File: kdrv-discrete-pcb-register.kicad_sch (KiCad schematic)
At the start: 3 parts, among them J1 Bus_PCI_Express_x16, J2 Bus_PCI_Express_x16, J3 Bus_PCI_Express_x16

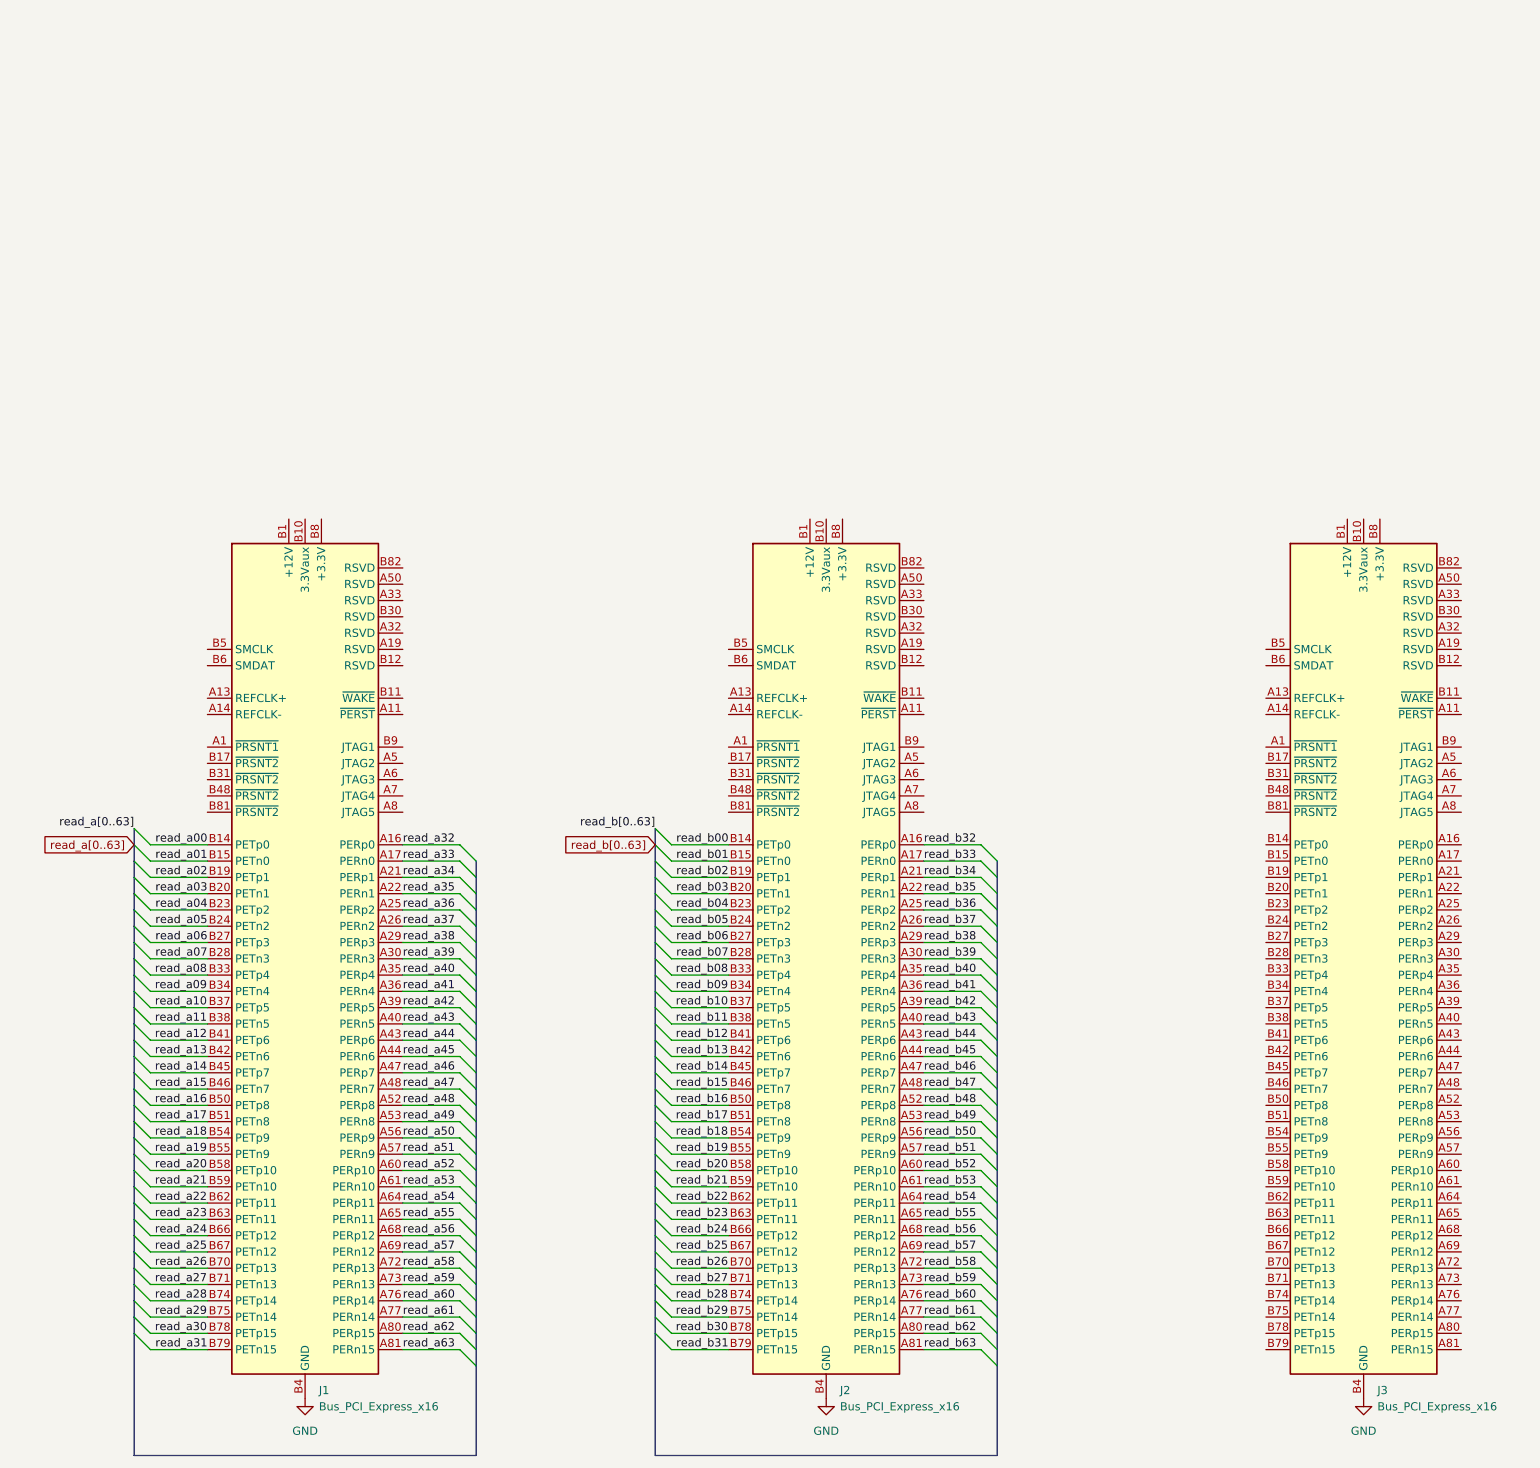
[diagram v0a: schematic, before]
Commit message: Schematic is pretty much complete.
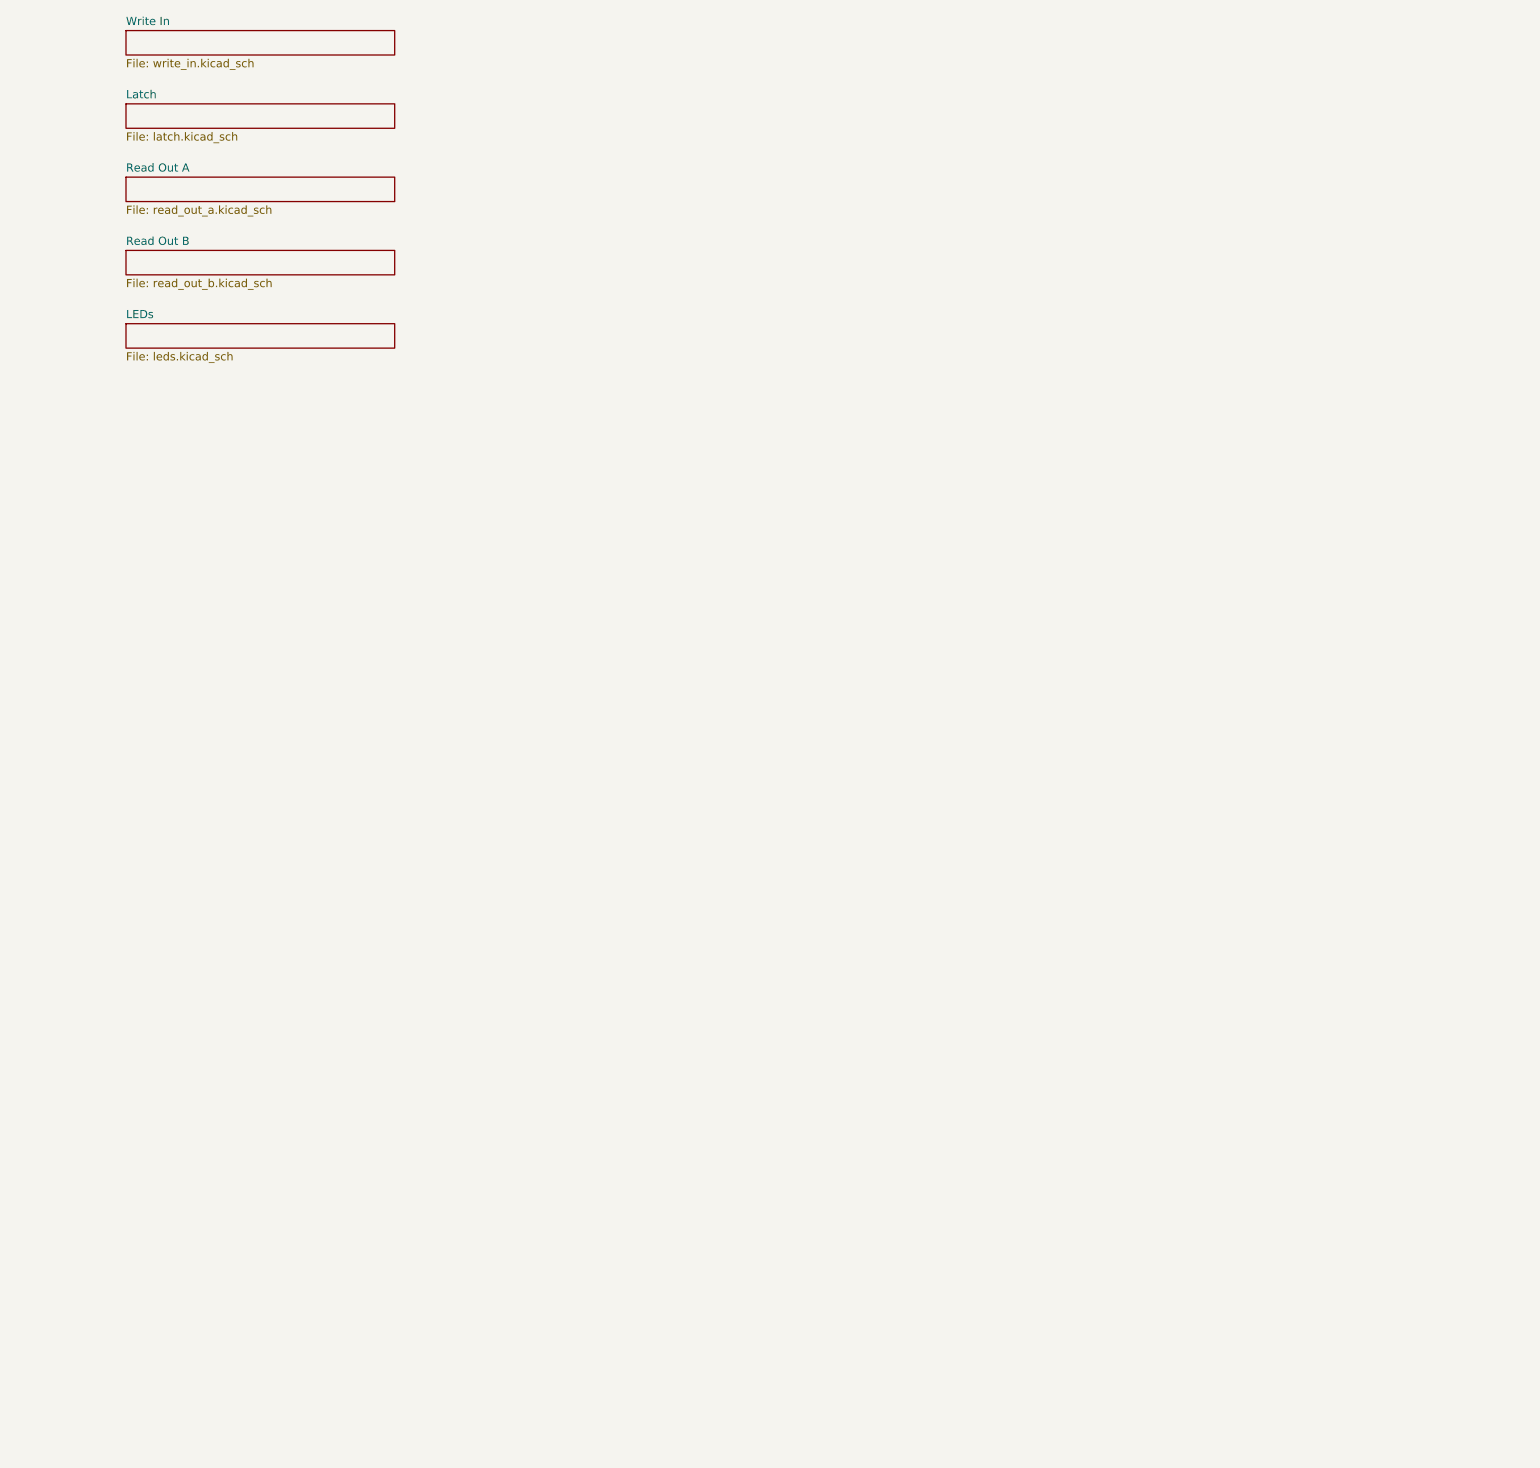
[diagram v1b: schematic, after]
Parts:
- removed J1, J2, J3: Bus_PCI_Express_x16, Connector_PCBEdge:BUS_PCIexpress_x16, symbol Connector:Bus_PCI_Express_x16
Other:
- added sheet LEDs (leds.kicad_sch)
- added sheet Latch (latch.kicad_sch)
- added sheet Read Out A (read_out_a.kicad_sch)
- added sheet Read Out B (read_out_b.kicad_sch)
- added sheet Write In (write_in.kicad_sch)
